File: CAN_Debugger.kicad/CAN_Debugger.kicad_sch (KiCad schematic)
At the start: 165 parts, among them J1 Conn_01x02, J15 RS-485, J16 RS-485, J2 Conn_01x04_MountingPin, J3 Conn_01x02, J4 Conn_01x16_Socket, J4 USB_C_Receptacle_USB2.0, J6 RS-485, J7 CAN, J8 CAN, J9 CAN, Q1 AO3400A, SW1 SW_Push, SW2 SW_Push, SW3 SW_Push, SW4 RotaryEncoder_Switch, U1 SN75176AD, U11 OPAMP2, U12 OPAMP3, U13 MT3608, U2 RY8411, U3 RS3236, U4 CH343P, U4 GS8332-SR, U5 SIT1042T/3, U6 RS3236, U7 INA186, U7 IP4220CZ6, U8 STM32G431CBUx, Y1 25MHz

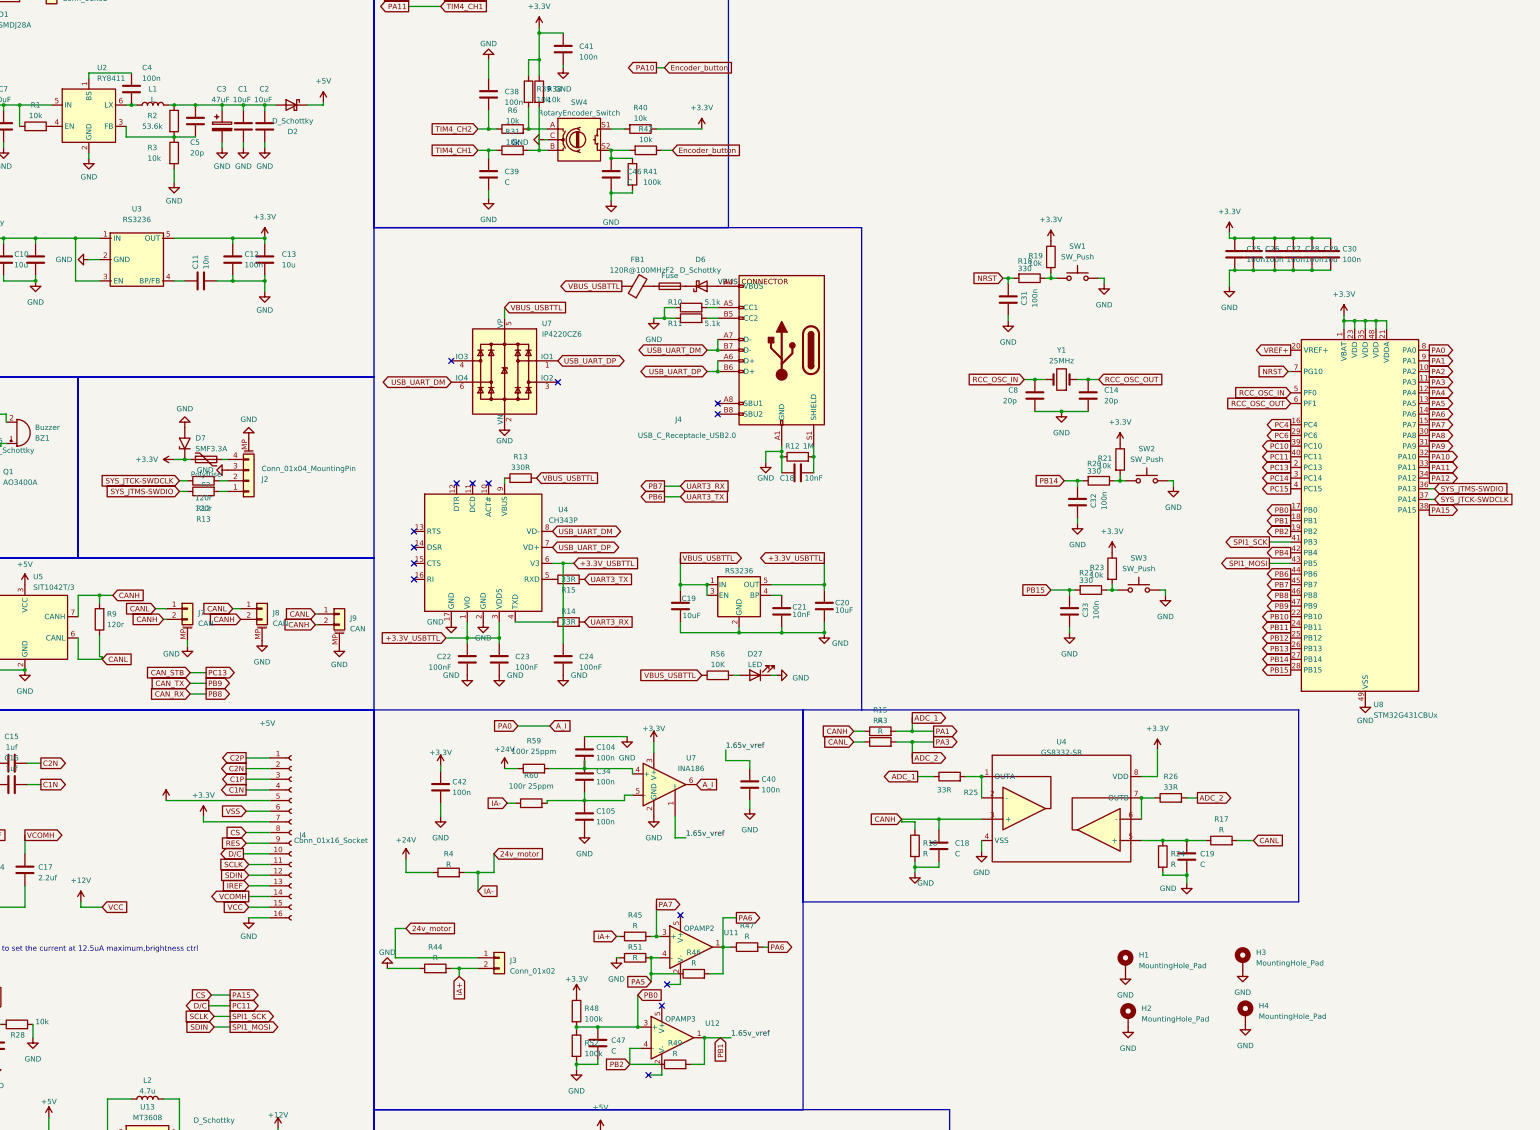
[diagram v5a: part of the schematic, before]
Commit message: update schematic
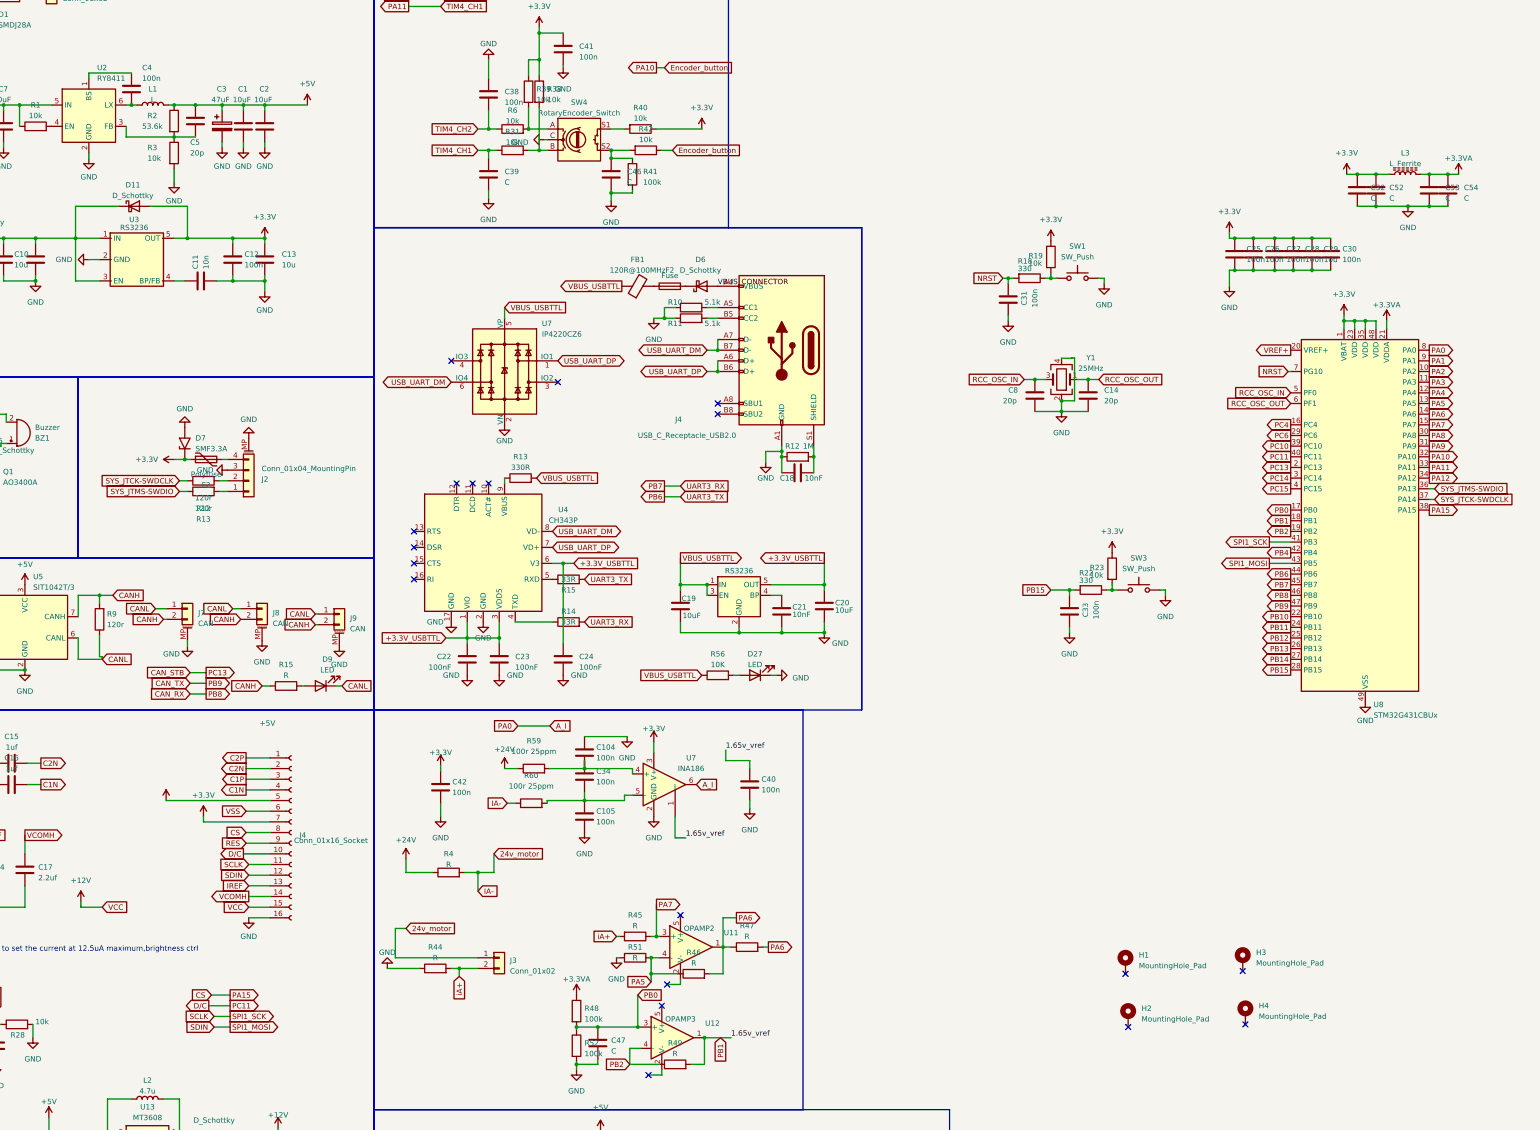
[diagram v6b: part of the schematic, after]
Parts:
- removed C18, C19: C, Capacitor_SMD:C_0603_1608Metric, symbol Device:C
- removed D2: D_Schottky, Diode_SMD:D_SMF, symbol Device:D_Schottky
- removed R16, R43: R, Resistor_SMD:R_0603_1608Metric, symbol Device:R
- removed R17, R24: R, Resistor_SMD:R_0603_1608Metric_Pad0.98x0.95mm_HandSolder, symbol Device:R
- removed R20: 330, Resistor_SMD:R_0603_1608Metric, symbol Device:R
- removed R21: 10k, Resistor_SMD:R_0603_1608Metric, symbol Device:R
- removed R25, R26: 33R, Resistor_SMD:R_0603_1608Metric_Pad0.98x0.95mm_HandSolder, symbol Device:R
- removed SW2: SW_Push, Button_Switch_SMD:SW_SPST_TL3342, symbol Switch:SW_Push
- removed U4: GS8332-SR, Package_SO:MSOP-8_3x3mm_P0.65mm, symbol 0_RM2023:GS8332-SR
- added C52, C53, C54: C, symbol Device:C
- added D11: D_Schottky, Diode_SMD:D_SMF, symbol Device:D_Schottky
- added D9: LED, LED_SMD:LED_0603_1608Metric, symbol Device:LED
- added L3: L_Ferrite, symbol Device:L_Ferrite
- C32: value 100n -> C; footprint Capacitor_SMD:C_0603_1608Metric -> (none)
- C48: footprint Inductor_SMD:L_0603_1608Metric -> Capacitor_SMD:C_1206_3216Metric
- L1: footprint Inductor_SMD:L_Bourns-SRN4018 -> Inductor_SMD:L_Sunlord_MWSA0402S
- L2: footprint Inductor_SMD:L_0603_1608Metric -> Inductor_SMD:L_Sunlord_MWSA0402S
- R49: now left out of the parts list
- Y1: footprint Crystal:Crystal_SMD_5032-2Pin_5.0x3.2mm -> Crystal:Crystal_SMD_3225-4Pin_3.2x2.5mm; symbol Device:Crystal -> Device:Crystal_GND24
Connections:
- net +3.3V: now also C32.1, C52.1, D11.2 (A), L3.1; no longer R48.1, U8.21 (VDDA)
- net +5V: now also C1.1, C2.1, C3.1, C5.1, L1.2, R2.1
- net CANL: now also D9.1 (K)
- net GND: now also C32.2, Y1.2, Y1.4, C52.2, C53.2, C54.2; no longer C32.1, H1.1, H2.1, H3.1, H4.1
- net PB14: no longer C32.2
- net RCC_OSC_IN: now also Y1.3; no longer Y1.2
- net at C10.1, C9.1, D3.1 (K)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: now also D11.1 (K)
- net ADC_1: no longer names the net of R15.2
- net ADC_1: now also D9.2 (A); no longer U8.9 (PA1)
- net ADC_2 renamed PA3
- new net +3.3VA: C53.1, C54.1, L3.2, R48.1, U8.21 (VDDA)
- new net PA1: U8.9 (PA1)
- no-connect marks 15 -> 19

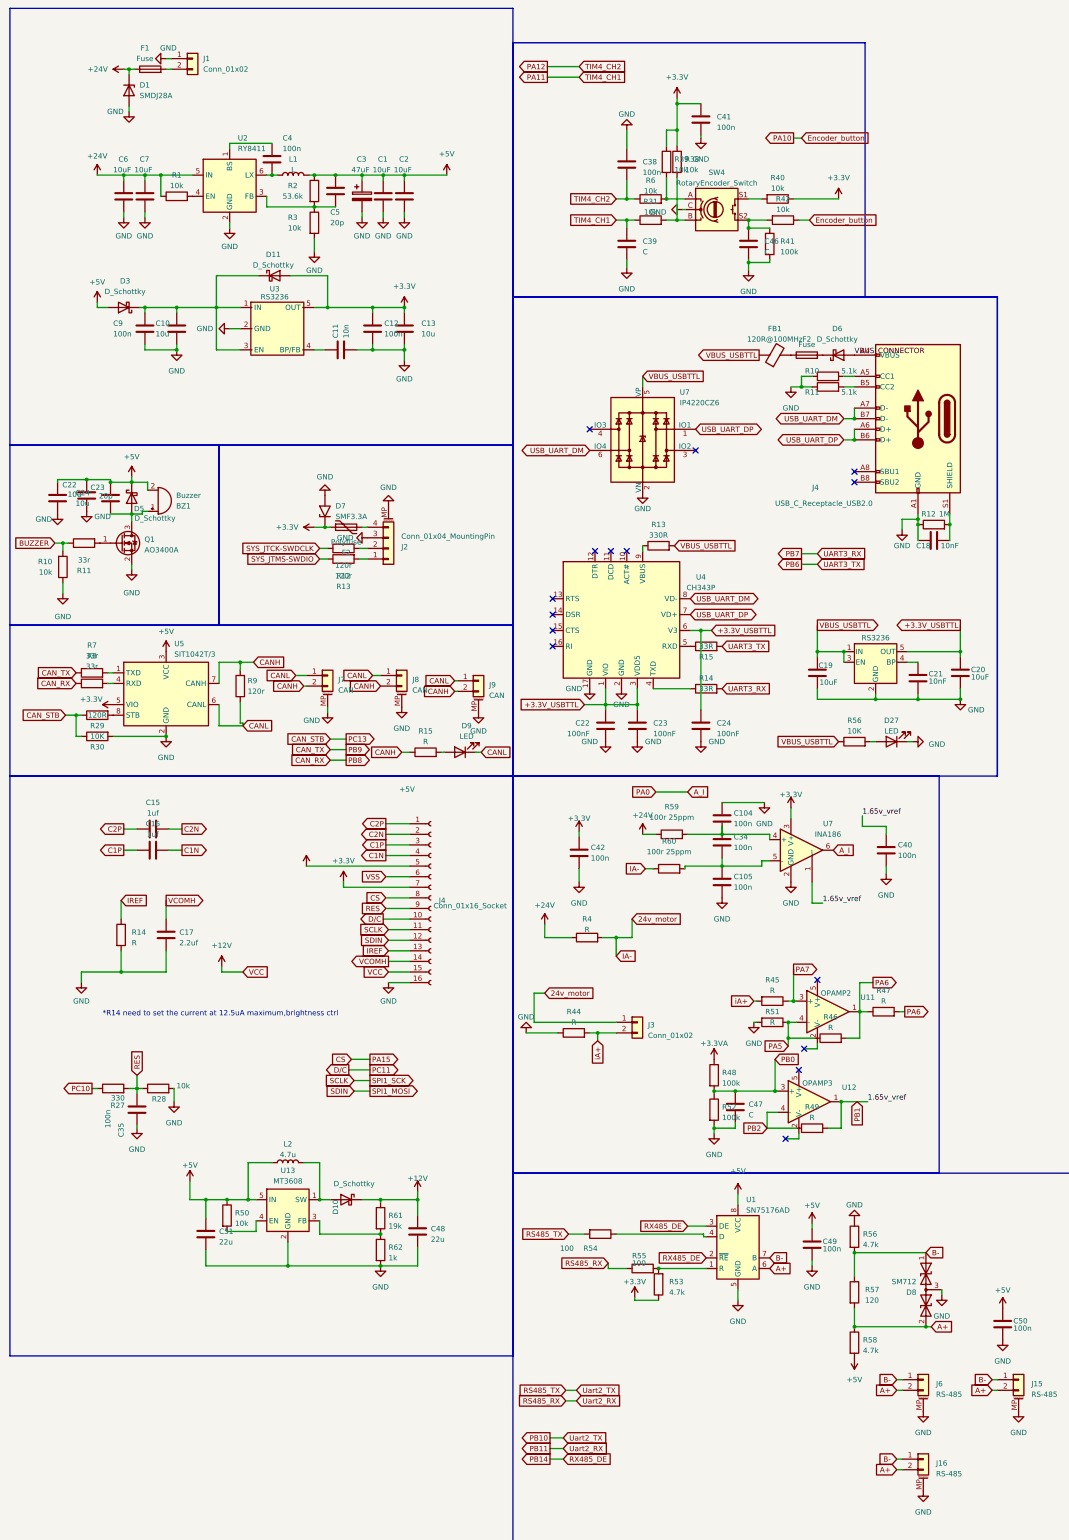
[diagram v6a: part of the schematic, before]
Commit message: Add Hardware Core; Add Handsolder QFN48 Footprint; Changes in schematic texts
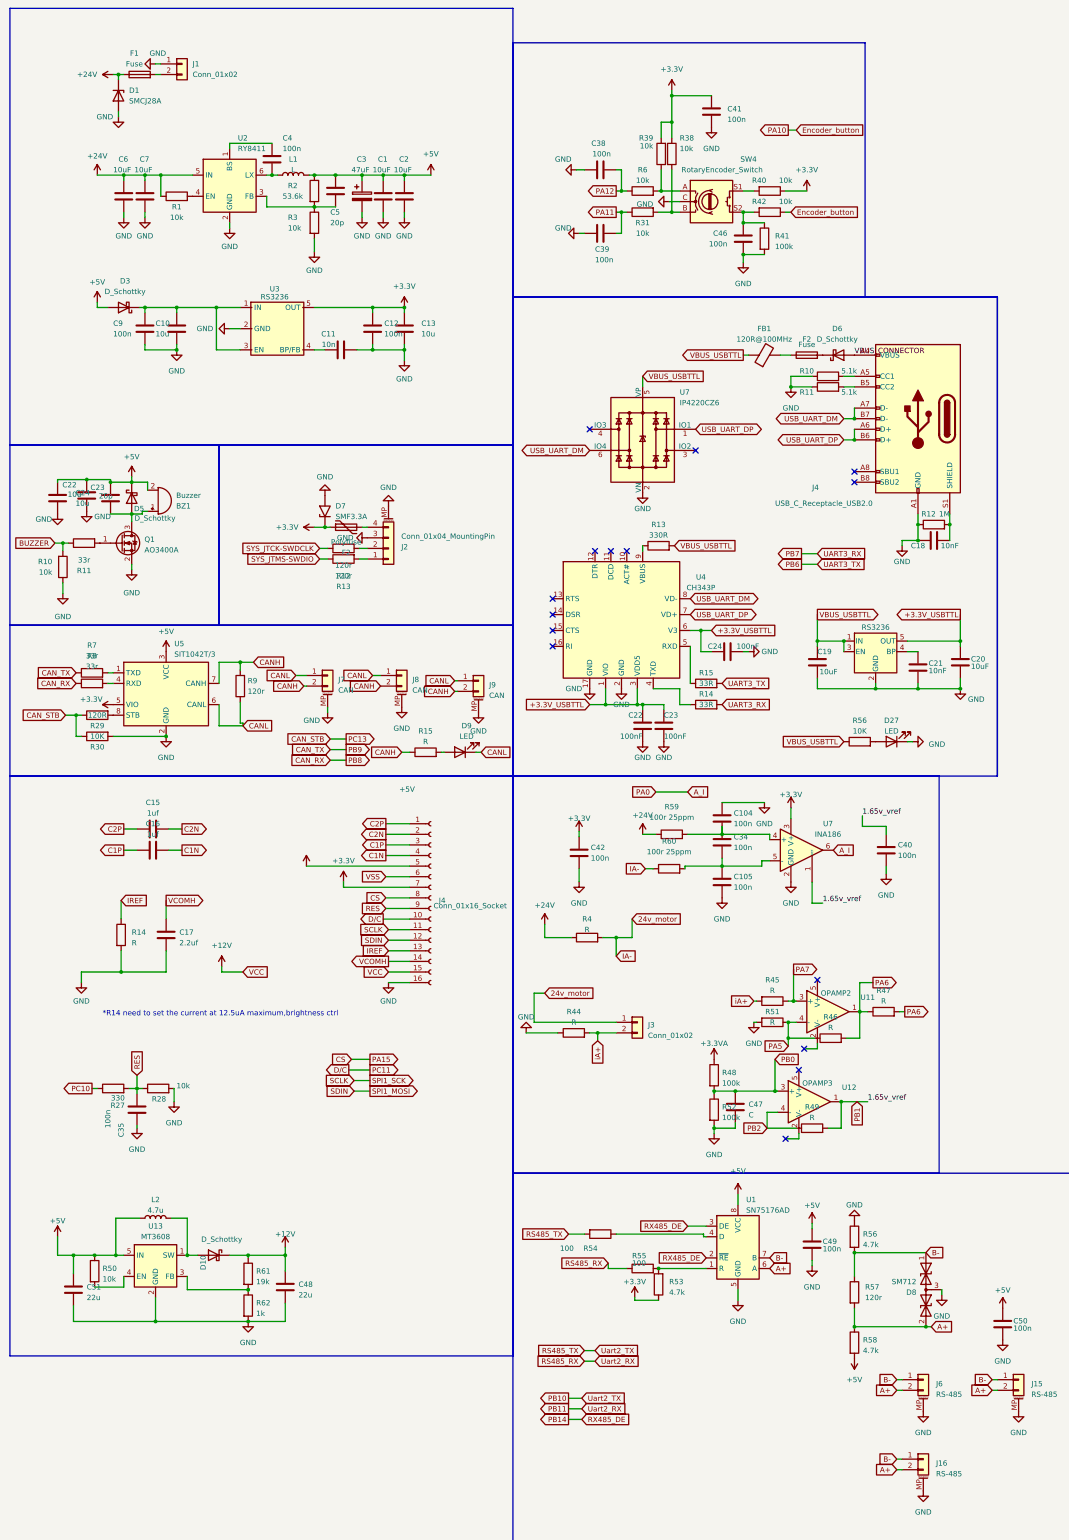
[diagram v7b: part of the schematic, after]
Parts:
- removed D11: D_Schottky, Diode_SMD:D_SMF, symbol Device:D_Schottky
- C39, C46: value C -> 100n
- D1: value SMDJ28A -> SMCJ28A
- R57: value 120 -> 120r
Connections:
- net +3.3V: now also R39.2; no longer R39.1
- net at R6.2, SW4.A: now also R39.1; no longer R39.2
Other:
- moved on the sheet: C19, C20, C21, C22, C23, C24, C38, C39, C41, C46, C48, C51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

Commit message: Update PCB layout
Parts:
- added C57, C58, C59, C70, C76, C88: 100n, Capacitor_SMD:C_0603_1608Metric, symbol Device:C
- added C80: 10u, Capacitor_SMD:C_0603_1608Metric, symbol Device:C
- added JP1: SolderJumper_2_Open, Jumper:SolderJumper-2_P1.3mm_Open_TrianglePad1.0x1.5mm, symbol Jumper:SolderJumper_2_Open
- added R16, R17, R21: 100k 25ppm, Resistor_SMD:R_0603_1608Metric, symbol Device:R
- added R20, R63: 33r, Resistor_SMD:R_0603_1608Metric, symbol Device:R
- added R24: 1k, Resistor_SMD:R_0603_1608Metric, symbol Device:R
- added R25: 10k 25ppm, Resistor_SMD:R_0603_1608Metric, symbol Device:R
- added RN1: R_Pack04, Resistor_SMD:R_Array_Convex_4x0603, symbol Device:R_Pack04
- added U14: GS8332-SR, Package_SO:SOIC-8_3.9x4.9mm_P1.27mm, symbol 0_RM2023:GS8332-SR
- C32, C52, C53, C54: footprint (none) -> Capacitor_SMD:C_0603_1608Metric
- L3: footprint (none) -> Inductor_SMD:L_0603_1608Metric
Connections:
- net PC6 is gone; now on net BUZZER: U8.29 (PC6)
- net +3.3V: no longer C29.1, C30.1
- net +3.3VA: now also C29.1, C30.1, C70.1, R16.2, U14.8 (VDD)
- net 24v_motor: now also R21.2
- net CANH: now also D9.1 (K); no longer R15.1
- net CANL: now also R15.1; no longer D9.1 (K)
- net CS: now also RN1.5 (R4.2); no longer U8.38 (PA15)
- net D/C: now also RN1.6 (R3.2); no longer U8.40 (PC11)
- net GND: now also C57.2, C59.2, C70.2, C76.2, C80.2, C88.1, R17.1, R25.1, U14.4 (VSS)
- net PB1: now also JP1.1 (A); no longer C40.1, R49.2, U12.1, U7.1 (REF)
- net PB6: now also R15.1; no longer R15.2
- net PC4: now also C88.2, R63.2
- net RCC_OSC_IN: now also C14.1, Y1.1; no longer C8.1, Y1.3
- net RCC_OSC_OUT: now also C8.1, Y1.3; no longer C14.1, Y1.1
- net SCLK: now also RN1.7 (R2.2); no longer U8.41 (PB3)
- net SDIN: now also RN1.8 (R1.2); no longer U8.43 (PB5)
- net at U4.5 (RXD): now also R15.2; no longer R15.1
- new net: C57.1, R16.1, R17.2, U14.3 (+)
- new net: R63.1, U14.6 (-), U14.7 (OUTB)
- new net: C58.1, R20.2, U14.1 (OUTA)
- new net: C58.2, R24.2, U14.2 (-)
- new net: C59.1, R21.1, R25.2, U14.5 (+)
- new net 1.65Vref: C40.1, C76.1, C80.1, JP1.2 (B), R20.1, R24.1, R49.2, U12.1, U7.1 (REF)
- new net PA15: RN1.4 (R4.1), U8.38 (PA15)
- new net PC11: RN1.3 (R3.1), U8.40 (PC11)
- new net SPI1_MOSI: RN1.1 (R1.1), U8.43 (PB5)
- new net SPI1_SCK: RN1.2 (R2.1), U8.41 (PB3)
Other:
- moved on the sheet: C14, C29, C30, C8, R15, Y1
